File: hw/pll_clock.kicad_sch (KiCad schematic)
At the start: 21 parts, among them J7 BNC, U7 5P49V5925, Y1 26MHz

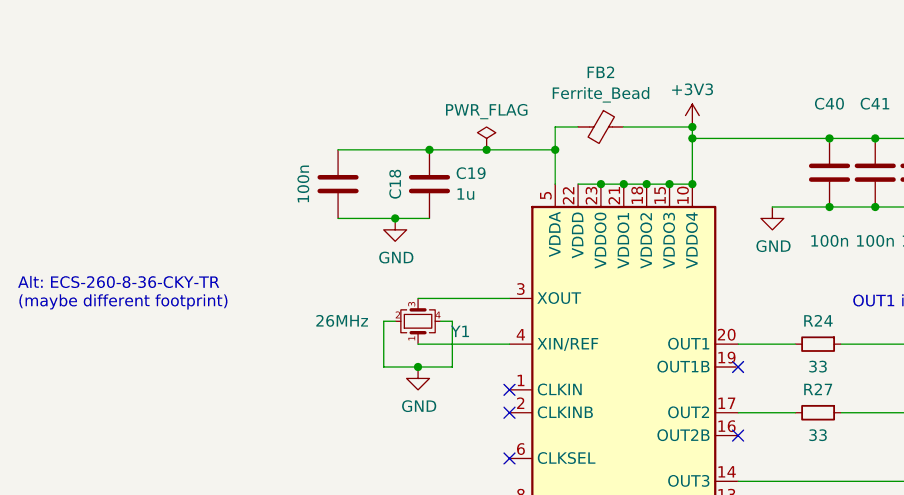
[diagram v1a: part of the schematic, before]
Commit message: updated some component values
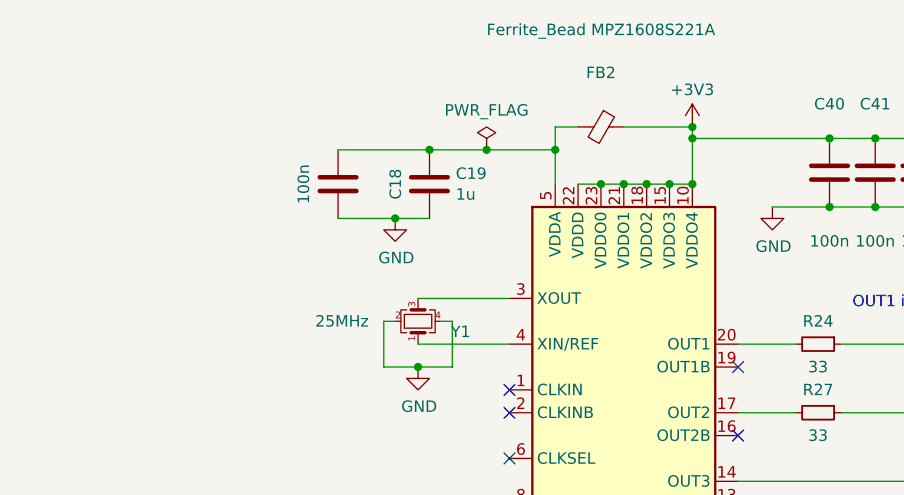
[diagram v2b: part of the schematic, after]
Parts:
- FB2: value Ferrite_Bead -> Ferrite_Bead MPZ1608S221A
- Y1: value 26MHz -> 25MHz; Part ABM10W-26.0000MHZ-8-B1U-T3 -> ABM10W-25.0000MHZ-8-B1U-T3
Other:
- note removed: "Alt: ECS-260-8-36-CKY-TR (maybe different footprint)"
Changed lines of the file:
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@@
     (stroke (width 0) (type default))
-  )
-  (text "Alt: ECS-260-8-36-CKY-TR\n(maybe different footprint)"
-    (at 74.93 69.85 0)
-    (effects (font (size 1.27 1.27)) (justify left bottom))
   )
   (text "TP1 is located close to C83. A 5P49V5925 chip\ncan be used instead of 5P49V6965; however, the\n5925 has only a single-ended output.\n - replace C63 by zero-ohm resistor\n - remove C83\n - ground ADC_CLK_N via TP1 -> ADC operates in SE\n   clocking mode"
@@
       (effects (font (size 1.27 1.27)) (justify left))
     )
-    (property "Value" "26MHz" (at 107.95 71.12 90)
+    (property "Value" "25MHz" (at 107.95 71.12 90)
       (effects (font (size 1.27 1.27)) (justify left))
     )
@@
       (effects (font (size 1.27 1.27)) hide)
     )
-    (property "Part" "ABM10W-26.0000MHZ-8-B1U-T3" (at 119.38 71.12 90)
+    (property "Part" "ABM10W-25.0000MHZ-8-B1U-T3" (at 119.38 71.12 90)
       (effects (font (size 1.27 1.27)) hide)
     )
@@
       (effects (font (size 1.27 1.27)))
     )
-    (property "Value" "Ferrite_Bead" (at 139.7 45.8216 90)
-      (effects (font (size 1.27 1.27)))
-    )
+    (property "Value" "Ferrite_Bead MPZ1608S221A" (at 139.7 38.735 90)
+      (effects (font (size 1.27 1.27)))
+    )

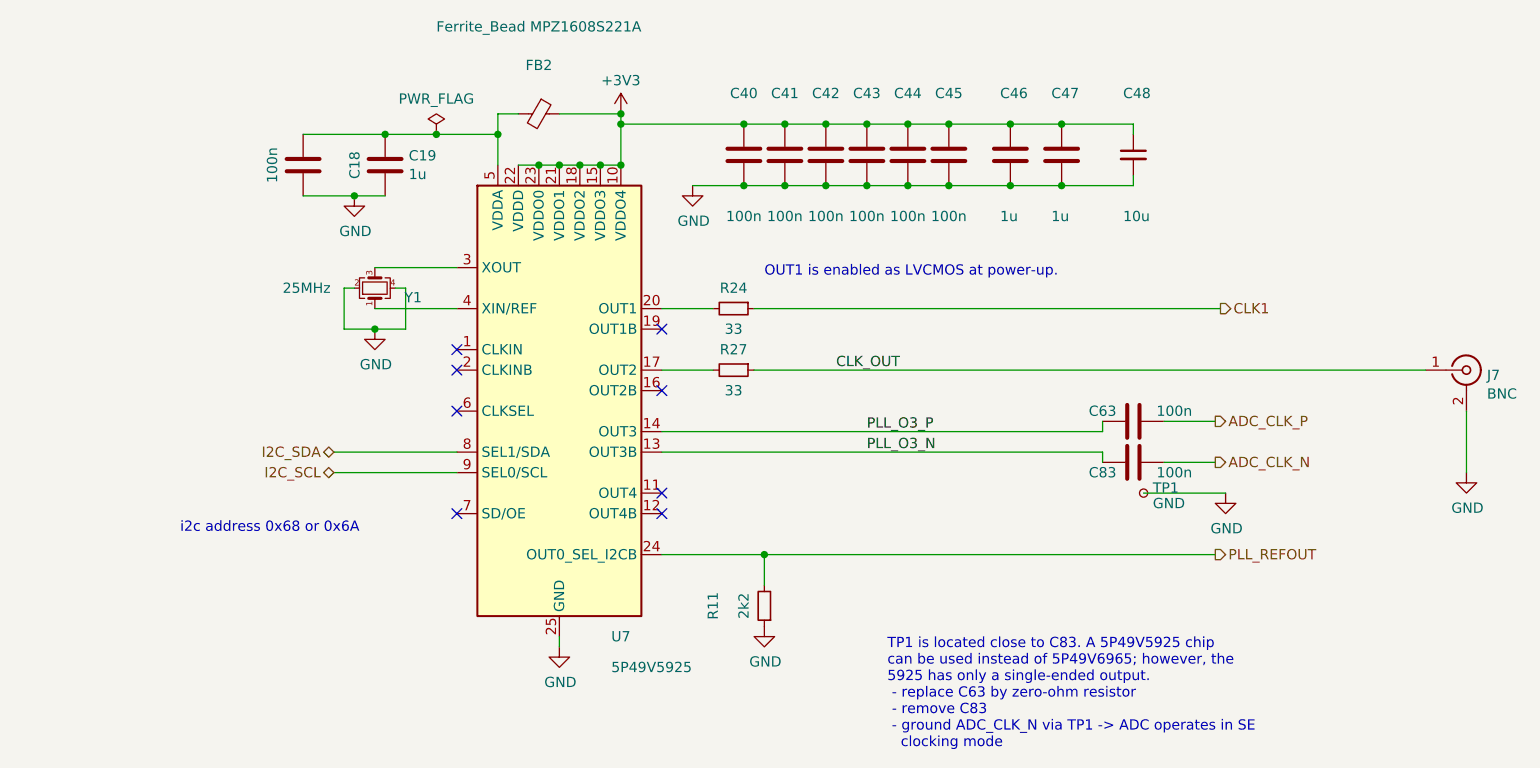
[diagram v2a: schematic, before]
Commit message: consolidated components to simplify BOM
(nothing actually changed but the symbols representing identical
components are now identical -> no more multiple BOM entries for
the same type of component).
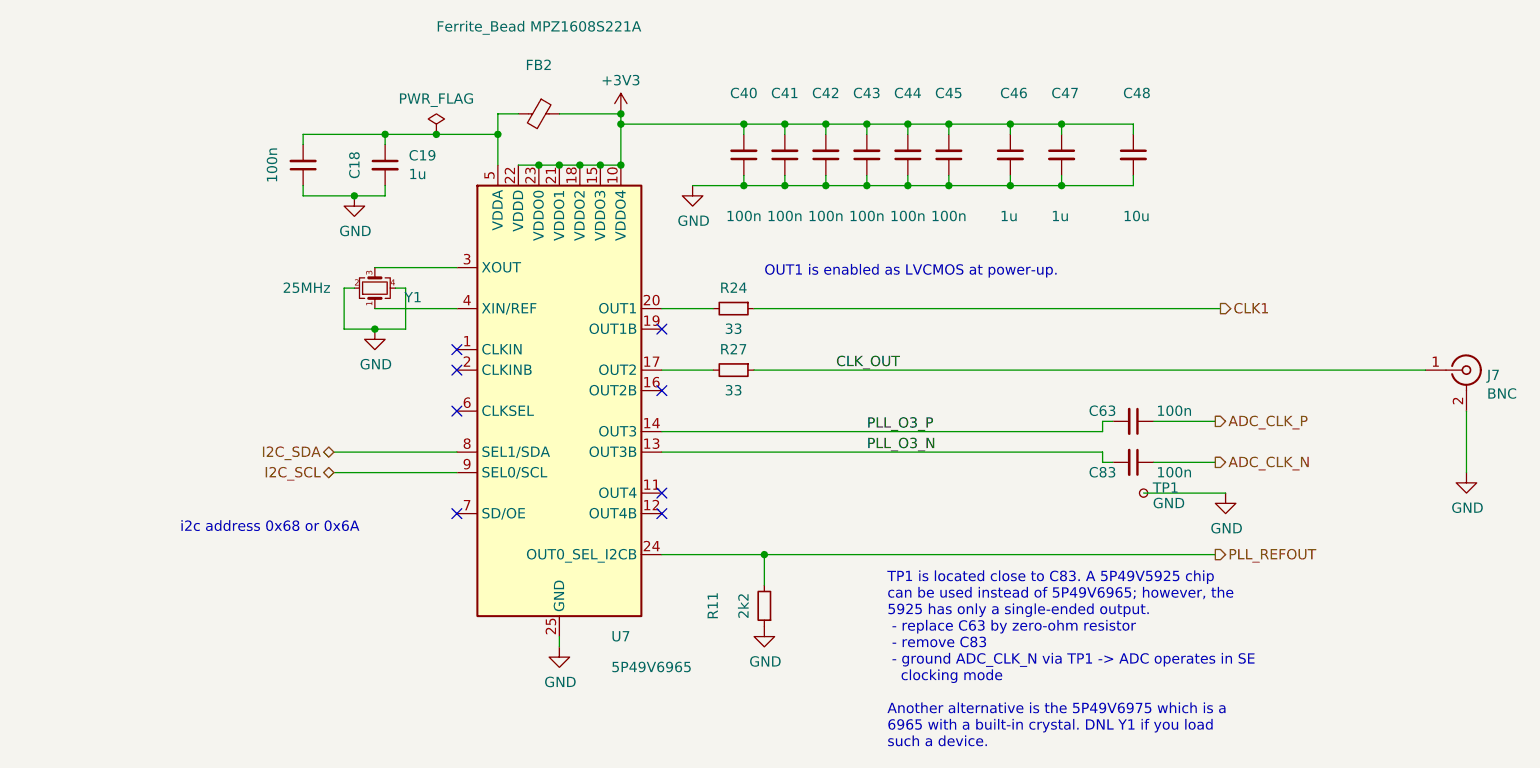
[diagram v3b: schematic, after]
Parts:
- C18, C40, C41, C42, C43, C44, C45, C63, C83: symbol fmc:100nF_603 -> Device:C_Small; Manufacturer (none) -> Samsung; Part (none) -> CL10B104KB8NFN
- C19, C46, C47: symbol fmc:1uF_805 -> Device:C_Small; Manufacturer (none) -> TDK; Part (none) -> CGA4J2X7R1C105K125AA
- C48: Manufacturer (none) -> Samsung; Part (none) -> CL31A106KPHNNNE
- U7: value 5P49V5925 -> 5P49V6965; Part 5P49V5925 -> 5P49V6965
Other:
- note added: "TP1 is located close to C83. A 5P49V5925 chip can be used instead of 5P49V6965; however, the 5925 has only a single-ended output. - replace C63 by zero-ohm resistor - remove C83 - ground ADC_CLK_N via TP1 -> ADC operates in SE clocking mode Another alternative is the 5P49V6975 which is a 6965 with a built-in crystal. DNL Y1 if you load such a device."
- note removed: "TP1 is located close to C83. A 5P49V5925 chip can be used instead of 5P49V6965; however, the 5925 has only a single-ended output. - replace C63 by zero-ohm resistor - remove C83 - ground ADC_CLK_N via TP1 -> ADC operates in SE clocking mode"

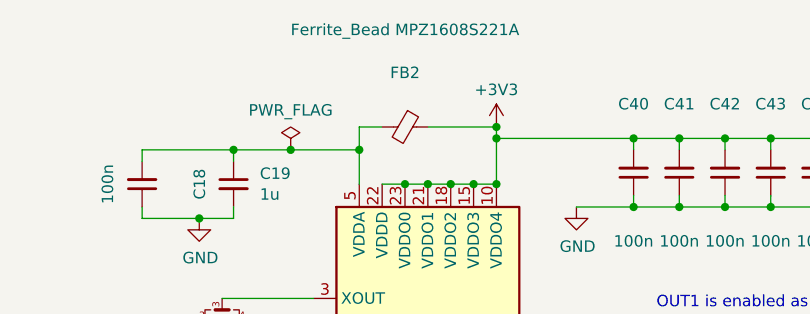
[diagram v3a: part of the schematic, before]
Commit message: consolidated ferrite beads (use same everywhere)
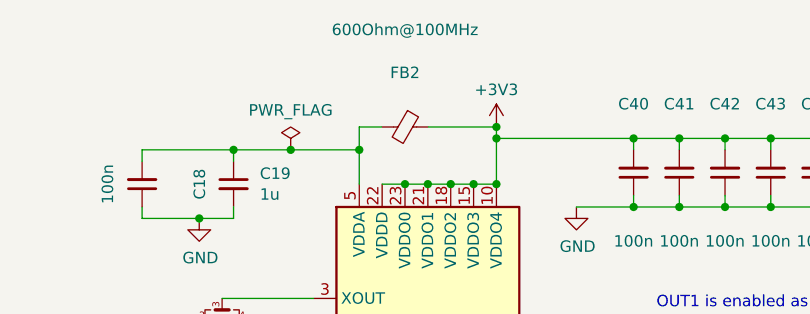
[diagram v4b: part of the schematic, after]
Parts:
- FB2: value Ferrite_Bead MPZ1608S221A -> 600Ohm@100MHz; Manufacturer TDK -> Laird; Part MPZ1608S221ATA00 -> MI0603J601R-10
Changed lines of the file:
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@@
       (effects (font (size 1.27 1.27)))
     )
-    (property "Value" "Ferrite_Bead MPZ1608S221A" (at 139.7 38.735 90)
+    (property "Value" "600Ohm@100MHz" (at 139.7 38.735 90)
       (effects (font (size 1.27 1.27)))
     )
@@
       (effects (font (size 1.27 1.27)) hide)
     )
-    (property "Part" "MPZ1608S221ATA00" (at 139.7 49.53 0)
+    (property "Part" "MI0603J601R-10" (at 139.7 49.53 0)
       (effects (font (size 1.27 1.27)) hide)
     )
-    (property "Manufacturer" "TDK" (at 139.7 49.53 0)
+    (property "Manufacturer" "Laird" (at 139.7 49.53 0)
       (effects (font (size 1.27 1.27)) hide)
     )

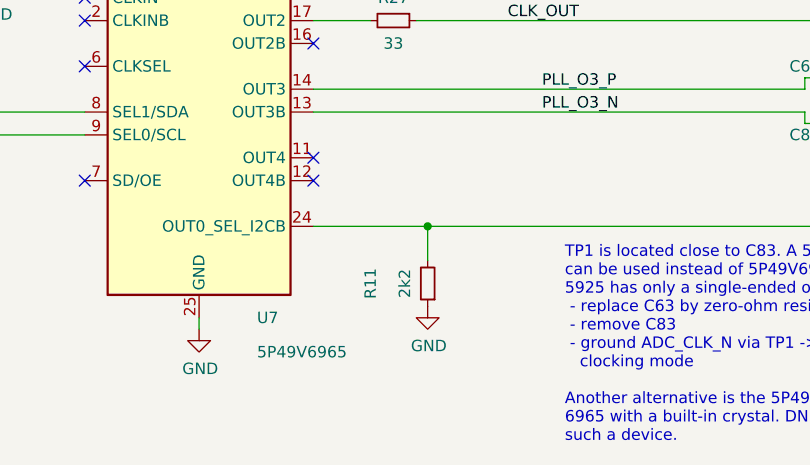
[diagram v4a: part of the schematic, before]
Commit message: Moved LEDs from +5V to 3V3. Removed LED driver FETs.
NOTE: the 3V3 connection is provisional and needs to be
reworked along with the redesign of the 5V net.

The temporary connections exist just to satisfy DRC for now.
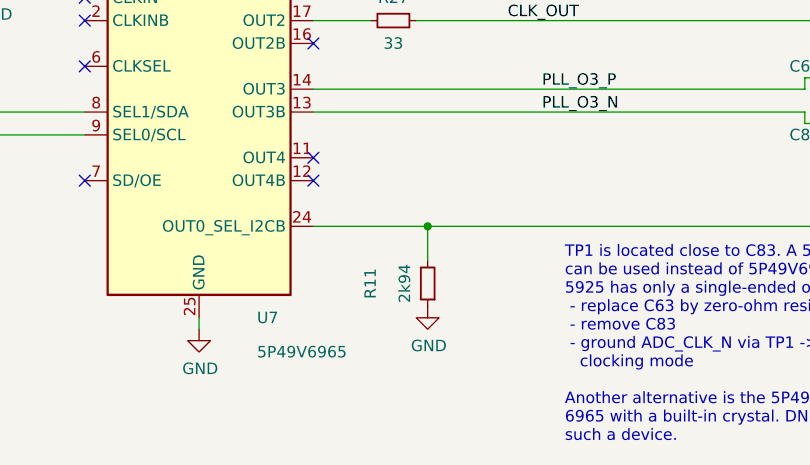
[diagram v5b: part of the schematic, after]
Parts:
- R11: value 2k2 -> 2k94
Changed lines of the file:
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@@
       (effects (font (size 1.27 1.27)))
     )
-    (property "Value" "2k2" (at 165.1 110.49 90)
+    (property "Value" "2k94" (at 165.1 110.49 90)
       (effects (font (size 1.27 1.27)))
     )

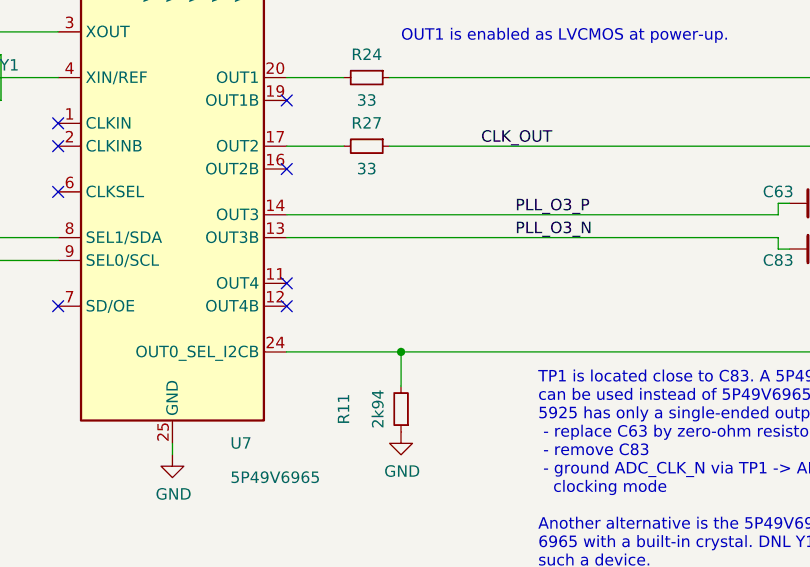
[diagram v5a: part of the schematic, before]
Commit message: Added (optional) connection from PLL output 4 to ulpi refclock.
Could spare the crystal oscillator...
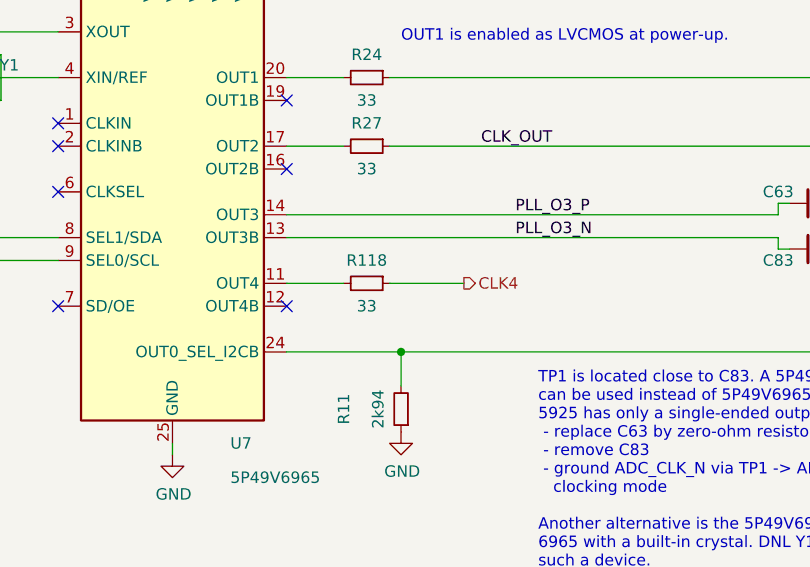
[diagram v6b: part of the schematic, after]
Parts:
- added R118: 33, Resistor_SMD:R_0603_1608Metric, symbol Device:R_Small
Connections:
- net at U7.11 (OUT4): now also R118.2
- new net CLK4: R118.1
- no-connect marks 8 -> 7
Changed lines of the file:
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@@
   (no_connect (at 129.54 99.06))
   (no_connect (at 129.54 86.36))
-  (no_connect (at 154.94 96.52))
   (no_connect (at 154.94 83.82))
   (no_connect (at 129.54 81.28))
@@
     (stroke (width 0) (type default))
   )
+  (wire (pts (xy 154.94 96.52) (xy 161.29 96.52))
+    (stroke (width 0) (type default))
+  )
   (wire (pts (xy 120.65 52.07) (xy 120.65 53.34))
     (stroke (width 0) (type default))
@@
   )
   (wire (pts (xy 134.62 49.53) (xy 137.16 49.53))
+    (stroke (width 0) (type default))
+  )
+  (wire (pts (xy 166.37 96.52) (xy 174.625 96.52))
     (stroke (width 0) (type default))
   )
@@
   (hierarchical_label "I2C_SDA" (shape bidirectional) (at 114.3 91.44 180) (fields_autoplaced)
     (effects (font (size 1.27 1.27)) (justify right))
+  )
+  (hierarchical_label "CLK4" (shape output) (at 174.625 96.52 0) (fields_autoplaced)
+    (effects (font (size 1.27 1.27)) (justify left))
   )
   (hierarchical_label "ADC_CLK_N" (shape output) (at 223.52 92.71 0) (fields_autoplaced)
@@
         )
       )
+    )
+  )
+  (symbol (lib_id "Device:R_Small") (at 163.83 96.52 270) (unit 1)
+    (in_bom yes) (on_board yes) (dnp no)
+    (property "Reference" "R118" (at 163.83 93.98 90)
+      (effects (font (size 1.27 1.27)))
+    )
+    (property "Value" "33" (at 163.83 99.06 90)
+      (effects (font (size 1.27 1.27)))
+    )
+    (property "Footprint" "Resistor_SMD:R_0603_1608Metric" (at 163.83 96.52 0)
+      (effects (font (size 1.27 1.27)) hide)
+    )
+    (property "Datasheet" "~" (at 163.83 96.52 0)
+      (effects (font (size 1.27 1.27)) hide)
+    )
+    (property "Part" "" (at 163.83 96.52 90)
+      (effects (font (size 1.27 1.27)) hide)
+    )
+    (property "Manufacturer" "" (at 163.83 96.52 90)
+      (effects (font (size 1.27 1.27)) hide)
+    )
+    (pin "1")
+    (pin "2")
+    (instances
+      (project "usbadc"
+        (path "/7c8a1f8d-8834-4c9b-aaae-1f231e9b09a1/00000000-0000-0000-0000-000060b16d71"
+          (reference "R118") (unit 1)
+        )
+      )

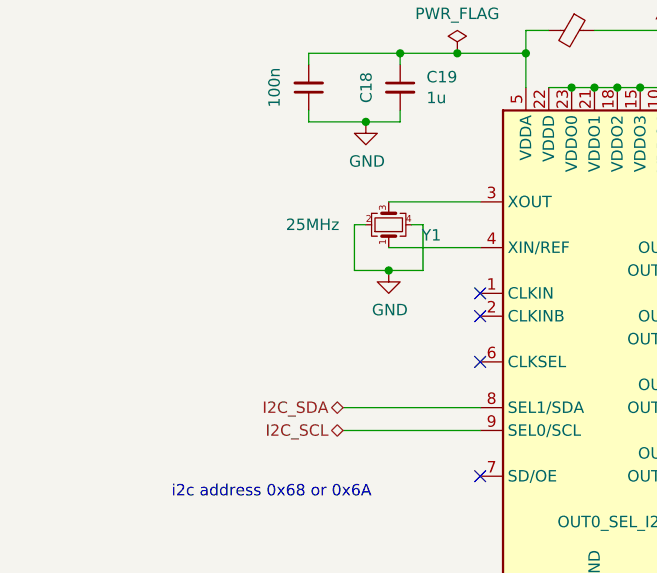
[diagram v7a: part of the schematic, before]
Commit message: added pll clock in divider from BNC, several pull-resistors
pull-resistors permit distinguishing board revisions.
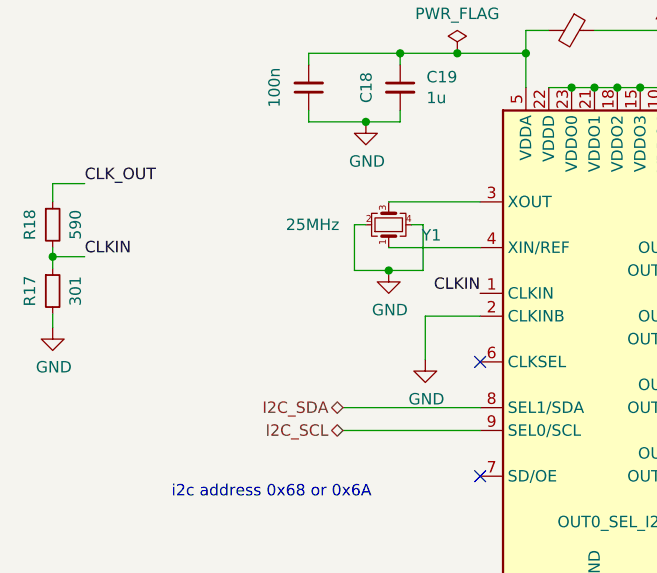
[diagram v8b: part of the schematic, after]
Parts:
- added R17: 301, Resistor_SMD:R_0603_1608Metric, symbol Device:R_Small
- added R18: 590, Resistor_SMD:R_0603_1608Metric, symbol Device:R_Small
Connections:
- net CLK_OUT: now also R18.1
- net GND: now also U7.2 (CLKINB), R17.2
- net CLKIN: now reaches U7.1 (CLKIN)
- net CLKIN: now also R17.1, R18.2
- no-connect marks 7 -> 5
